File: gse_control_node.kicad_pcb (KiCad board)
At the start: 4 copper layers, 65 x 65 mm, 119 parts, among them J1 Screw_Terminal_01x02, J10 Conn_01x02, J2 Conn_01x04, J3 Conn_01x04, J4 Conn_02x01, J5 USB_C_Receptacle_USB2.0_16P, J6 Conn_01x04, J7 Conn_01x02, J8 Conn_01x02, J9 Conn_01x02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

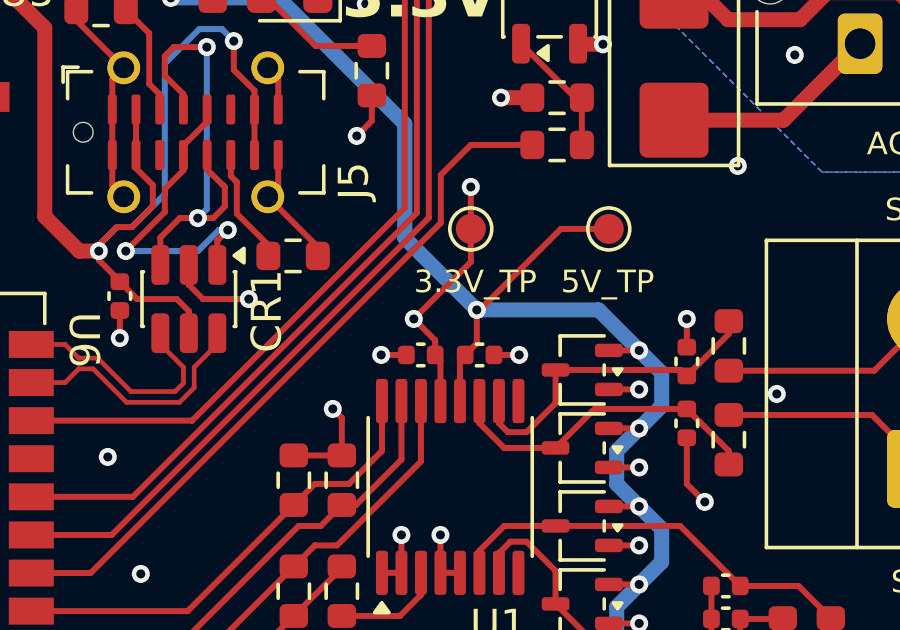
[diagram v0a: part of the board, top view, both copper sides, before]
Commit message: move up ads112c04 capacitors further from pins for easier handsoldering
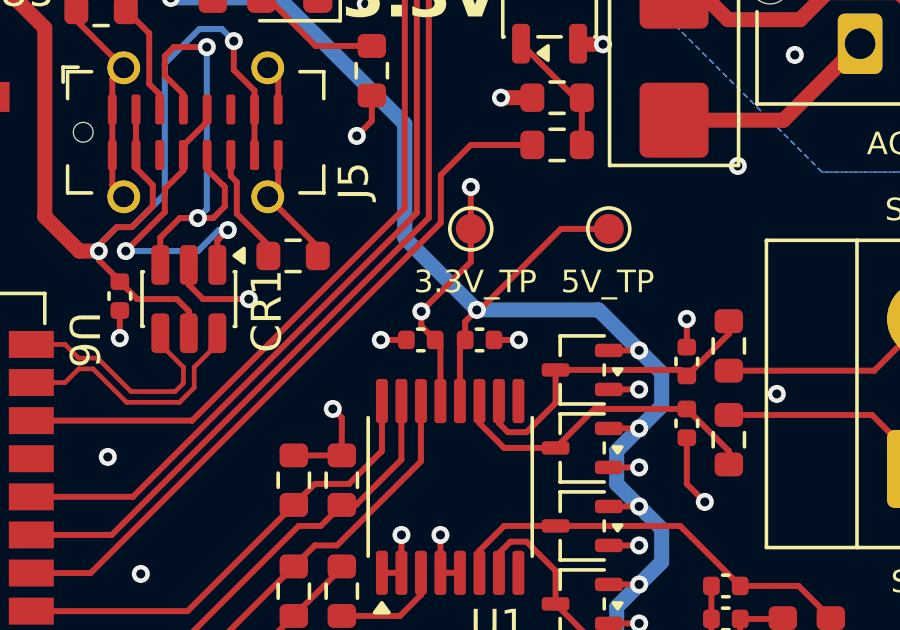
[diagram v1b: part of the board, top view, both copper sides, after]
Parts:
- moved C1 0.50 mm to (106.0, 63.5)
- moved C2 0.50 mm to (108.0, 63.5)
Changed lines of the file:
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@@
 	(footprint "Capacitor_SMD:C_0402_1005Metric"
 		(layer "F.Cu")
-		(at 107.992499 64)
+		(at 107.992499 63.5)
 		(descr "Capacitor SMD 0402 (1005 Metric), square (rectangular) end terminal, IPC-7351 nominal, (Body size source: IPC-SM-782 page 76, https://www.pcb-3d.com/wordpress/wp-content/uploads/ipc-sm-782a_amendment_1_and_2.pdf)")
 		(tags "capacitor")
@@
 	(footprint "Capacitor_SMD:C_0402_1005Metric"
 		(layer "F.Cu")
-		(at 106.032499 64 180)
+		(at 106.032499 63.5 180)
 		(descr "Capacitor SMD 0402 (1005 Metric), square (rectangular) end terminal, IPC-7351 nominal, (Body size source: IPC-SM-782 page 76, https://www.pcb-3d.com/wordpress/wp-content/uploads/ipc-sm-782a_amendment_1_and_2.pdf)")
 		(tags "capacitor")
@@
 	)
 	(segment
+		(start 108.472499 63.5)
+		(end 109.3 63.5)
+		(width 0.2)
+		(layer "F.Cu")
+		(net "GND")
+	)
+	(segment
 		(start 112.299999 67.75)
 		(end 113.312499 67.75)
@@
 	)
 	(segment
-		(start 105.552499 64)
-		(end 104.712499 64)
-		(width 0.2)
-		(layer "F.Cu")
-		(net "GND")
-	)
-	(segment
 		(start 114.9 63.74)
 		(end 114.9 62.8)
@@
 	)
 	(segment
-		(start 108.472499 64)
-		(end 109.312499 64)
-		(width 0.2)
-		(layer "F.Cu")
-		(net "GND")
-	)
-	(segment
 		(start 100.93 54.427918)
 		(end 101.28 54.777918)
@@
 	)
 	(segment
+		(start 105.552499 63.5)
+		(end 104.7 63.5)
+		(width 0.2)
+		(layer "F.Cu")
+		(net "GND")
+	)
+	(segment
 		(start 84.52 51.8)
 		(end 86 51.8)
@@
 	)
 	(via
+		(at 104.7 63.5)
+		(size 0.6)
+		(drill 0.3)
+		(layers "F.Cu" "B.Cu")
+		(net "GND")
+	)
+	(via
 		(at 73.7 66.1)
 		(size 0.6)
@@
 	)
 	(via
-		(at 104.712499 64)
-		(size 0.6)
-		(drill 0.3)
-		(layers "F.Cu" "B.Cu")
-		(net "GND")
-	)
-	(via
 		(at 99.1 79.57)
 		(size 0.6)
@@
 	)
 	(via
+		(at 109.3 63.5)
+		(size 0.6)
+		(drill 0.3)
+		(layers "F.Cu" "B.Cu")
+		(net "GND")
+	)
+	(via
 		(at 116.6 40.7)
 		(size 0.6)
@@
 	)
 	(via
-		(at 109.312499 64)
-		(size 0.6)
-		(drill 0.3)
-		(layers "F.Cu" "B.Cu")
-		(net "GND")
-	)
-	(via
 		(at 109.4 22)
 		(size 0.6)
@@
 	)
 	(segment
-		(start 107.9 62.5)
-		(end 107.9 63.612499)
+		(start 107.337499 65.5375)
+		(end 107.337499 63.675)
 		(width 0.2)
 		(layer "F.Cu")
@@
 	)
 	(segment
-		(start 112.299999 66.45)
-		(end 113.312499 66.45)
+		(start 107.337499 63.675)
+		(end 107.512499 63.5)
 		(width 0.2)
 		(layer "F.Cu")
@@
 	)
 	(segment
-		(start 107.337499 65.5375)
-		(end 107.337499 64.175)
+		(start 112.299999 66.45)
+		(end 113.312499 66.45)
 		(width 0.2)
 		(layer "F.Cu")
@@
 	)
 	(segment
+		(start 107.512499 62.887501)
+		(end 107.9 62.5)
+		(width 0.2)
+		(layer "F.Cu")
+		(net "+5V")
+	)
+	(segment
 		(start 98.475 51.325)
 		(end 97.7 52.1)
@@
 	)
 	(segment
-		(start 107.337499 64.175)
-		(end 107.512499 64)
+		(start 107.512499 63.5)
+		(end 107.512499 62.887501)
 		(width 0.2)
 		(layer "F.Cu")
@@
 	)
 	(segment
-		(start 107.9 63.612499)
-		(end 107.512499 64)
-		(width 0.2)
-		(layer "F.Cu")
-		(net "+5V")
-	)
-	(segment
 		(start 97.3 48.55)
 		(end 98.475 49.725)
@@
 	)
 	(segment
-		(start 71.704958 49.925)
-		(end 71.704958 50.704958)
+		(start 106.687499 63.675)
+		(end 106.512499 63.5)
 		(width 0.2)
 		(layer "F.Cu")
@@
 	)
 	(segment
-		(start 106.687499 64.175)
-		(end 106.512499 64)
+		(start 106.05 62.55)
+		(end 107.7 60.9)
+		(width 0.2)
+		(layer "F.Cu")
+		(net "+3.3V")
+	)
+	(segment
+		(start 71.704958 49.925)
+		(end 71.704958 50.704958)
 		(width 0.2)
 		(layer "F.Cu")
@@
 	)
 	(segment
-		(start 73.7 52.7)
-		(end 79.8 52.7)
+		(start 106.687499 65.5375)
+		(end 106.687499 63.675)
 		(width 0.2)
 		(layer "F.Cu")
@@
 	)
 	(segment
-		(start 106.687499 65.5375)
-		(end 106.687499 64.175)
+		(start 73.7 52.7)
+		(end 79.8 52.7)
 		(width 0.2)
 		(layer "F.Cu")
@@
 	)
 	(segment
-		(start 106.512499 63.512499)
-		(end 105.8 62.8)
+		(start 106.05 63.037501)
+		(end 106.512499 63.5)
 		(width 0.2)
 		(layer "F.Cu")
@@
 	)
 	(segment
-		(start 107.7 59.8)
-		(end 107.7 60.9)
+		(start 94.635 78.91)
+		(end 94.715 78.99)
 		(width 0.2)
 		(layer "F.Cu")
@@
 	)
 	(segment
-		(start 94.635 78.91)
-		(end 94.715 78.99)
+		(start 107.7 60.9)
+		(end 107.7 59.8)
 		(width 0.2)
 		(layer "F.Cu")
@@
 	)
 	(segment
-		(start 107.7 60.9)
-		(end 105.8 62.8)
+		(start 106.05 62.55)
+		(end 106.05 63.037501)
 		(width 0.2)
 		(layer "F.Cu")
@@
 	)
 	(segment
-		(start 106.512499 64)
-		(end 106.512499 63.512499)
-		(width 0.2)
-		(layer "F.Cu")
-		(net "+3.3V")
-	)
-	(segment
 		(start 104.4 55.35)
 		(end 104.4 56.2)
@@
 	)
 	(via
-		(at 105.8 62.8)
+		(at 106.05 62.55)
 		(size 0.6)
 		(drill 0.3)
@@
 		(members "0713b475-f5cb-4c27-85e3-ad1de07ab9aa" "077e1e74-6f91-4637-9c72-50ae116940d0"
 			"09fb94bb-8471-4aec-ad5d-a9e6f7ed850c" "143357c3-ebe5-4e68-bb4f-053ab14f5365"
-			"1611942c-b6f4-400d-942c-48b3fd8efb8b" "2002362c-b7c0-435e-b928-a278ebd1ba91"
-			"254d465c-a598-4fa1-838f-c53555367d58" "26810a1b-9afc-4230-aa9a-717d25e7bf46"
+			"1611942c-b6f4-400d-942c-48b3fd8efb8b" "18de1a66-394e-45ff-8f65-4990c2640ed2"
+			"2002362c-b7c0-435e-b928-a278ebd1ba91" "26810a1b-9afc-4230-aa9a-717d25e7bf46"
 			"272b0b43-69c4-45c3-a902-39b13e856481" "3392c1c7-c6f3-47a8-a50d-0791db8bd6ba"
 			"35487309-e541-48d0-83e2-fdf5931405a9" "398871a5-91ec-4523-b6c2-31a6d168fd13"
 			"3992ca7f-4747-4014-b0d3-b52654d03022" "3a4d2a50-53e1-4501-b2b1-020b92b24701"
-			"4031506d-cd5c-474b-aded-242a9de5b808" "4bb322c4-beaa-4428-8206-724f55f07d49"
+			"3ca64c91-c041-451d-aa41-0b8179a51e5b" "4031506d-cd5c-474b-aded-242a9de5b808"
+			"4ae5ce71-c6d8-4e7c-b337-34813efee1bc" "4bb322c4-beaa-4428-8206-724f55f07d49"
 			"520842bf-d7f1-45f1-a857-1e2e2b3e0304" "53271790-ca79-482e-aa70-61861ad501a4"
 			"5ac32f9c-315f-4e1c-86a3-f0cc58c834f3" "5ba14bdf-6ad9-4dd0-868b-07183184e65b"
 			"60ee43a8-b7f1-4438-ace5-67193ee89a17" "6a3f31a3-fe63-4587-9a30-071251119eca"
 			"6b6c3120-d685-45bb-883f-7689f5c635ba" "77c11dec-9216-45a1-beb1-ecd6b7c83a28"
-			"79d439f1-bc39-4da3-8bfa-e40741087e2c" "7f6941e2-e005-46d9-a4d8-e668f29aadfa"
-			"7fb87c2d-13ab-42b9-a622-50f20d7c8d91" "85811859-a147-483f-ae9c-36d4455d3eb6"
+			"79d439f1-bc39-4da3-8bfa-e40741087e2c" "7fb87c2d-13ab-42b9-a622-50f20d7c8d91"
+			"813fed4b-3560-48dc-b9dc-4773828fcd3b" "85811859-a147-483f-ae9c-36d4455d3eb6"
 			"874789a6-e4f6-4d20-96b9-63f47ce8a054" "89242e3a-437f-4c51-836e-c2bfc0d14e6b"
-			"8c5af611-fac6-4ee7-9db9-3087e55b4cbc" "9520423f-e2b5-4333-b303-308e31356465"
-			"9679f33c-0414-4287-bc77-a4bfba0f9619" "972f63cd-ad98-4fb9-bbfb-7680c819cf8f"
-			"97ef5fcd-715e-4292-849d-59b79a742a7d" "99416f0b-bd1e-450c-9a2d-39476234f809"
-			"99a3ca92-a9b4-4f3a-8894-e1c4da141f22" "9a605955-d230-4d70-9ac7-4ab602a980e3"
-			"a047faab-255e-4ef1-bdc6-788e9bc43326" "a1ecc4fa-a627-4f55-9ba0-37c7803925a8"
+			"8b92bc17-2e35-45b4-ac6d-edc5b158a71e" "9520423f-e2b5-4333-b303-308e31356465"
+			"9679f33c-0414-4287-bc77-a4bfba0f9619" "97ef5fcd-715e-4292-849d-59b79a742a7d"
+			"99416f0b-bd1e-450c-9a2d-39476234f809" "99a3ca92-a9b4-4f3a-8894-e1c4da141f22"
+			"9a605955-d230-4d70-9ac7-4ab602a980e3" "a047faab-255e-4ef1-bdc6-788e9bc43326"
 			"a93fd3e5-3a84-4405-ae40-05b572e65529" "a9b2d57a-f670-4513-b9c0-c2dc32cccd4e"
-			"aa20b915-049c-41ac-bf38-724fe6be948c" "aff2acdf-d84c-4d91-859b-550af43d1e9b"
+			"ad331356-d70b-4977-b70c-951d6688ec29" "aff2acdf-d84c-4d91-859b-550af43d1e9b"
 			"b0897651-7570-48f1-acde-4cc7863531c8" "bac0bc6e-03ea-4ccd-a2d3-603e4a49b3d7"
-			"bdf58728-7c54-4d66-8e71-7c2b8beb86f8" "c3e717e2-7834-47ee-ac64-8a312146c262"
-			"c494923c-e162-4fc7-a0e4-078a73375c22" "c52fd37b-f8b4-4782-bbd6-512d36cd1355"
-			"c5ae6679-79b9-4580-9dbc-c82893933102" "c667d184-ed5d-4410-9b14-25c8bdc7dc27"
-			"c784093f-aa9b-4f53-902b-9be59066781f" "c85fb981-ea2f-4e3b-af4e-8b51bd8042af"
-			"c93e094e-23ad-4496-a67c-0f8ea6effcd8" "cc0d71a9-384e-4854-bdc0-0d0361614c1a"
-			"cdb0dd8d-516c-49c6-8032-b546fb987add" "d0cbf0f5-bd98-42b9-baca-ec8107ff06dc"
-			"d2acdac1-c997-4b5b-92bd-a9f6b2d041a3" "d6f2acbf-eac1-48da-b50e-1cdd310e12a0"
-			"d89bfdb0-187b-4b25-a7b7-b023acbaa4b4" "da27c5d9-14f2-48bc-81b8-29e3cf13fe25"
-			"dcbbba95-6765-4085-874d-df7959760735" "e5ad27bf-e527-44fb-aa32-76ae20692841"
+			"bdf58728-7c54-4d66-8e71-7c2b8beb86f8" "c00c2267-045f-4dc7-8730-456783d7cecc"
+			"c3e717e2-7834-47ee-ac64-8a312146c262" "c494923c-e162-4fc7-a0e4-078a73375c22"
+			"c52fd37b-f8b4-4782-bbd6-512d36cd1355" "c5ae6679-79b9-4580-9dbc-c82893933102"
+			"c667d184-ed5d-4410-9b14-25c8bdc7dc27" "c784093f-aa9b-4f53-902b-9be59066781f"
+			"c85fb981-ea2f-4e3b-af4e-8b51bd8042af" "c93e094e-23ad-4496-a67c-0f8ea6effcd8"
+			"cc0d71a9-384e-4854-bdc0-0d0361614c1a" "cdb0dd8d-516c-49c6-8032-b546fb987add"
+			"d0cbf0f5-bd98-42b9-baca-ec8107ff06dc" "d2acdac1-c997-4b5b-92bd-a9f6b2d041a3"
+			"d6f2acbf-eac1-48da-b50e-1cdd310e12a0" "d89bfdb0-187b-4b25-a7b7-b023acbaa4b4"
+			"da27c5d9-14f2-48bc-81b8-29e3cf13fe25" "dcbbba95-6765-4085-874d-df7959760735"
 			"e70306a6-08d0-488c-bf4f-7f69efa03470" "e85a9e07-8c9b-44bd-915f-96d6cd51afa4"
-			"e91782cf-deaf-4542-8095-f2d6c775d17d" "eea5b277-e46b-4c3b-8d5c-9d3e61cdf2b4"
-			"ef3803de-90ad-46b6-948b-407f3d22f1e5" "eff16b14-496b-40bc-aeac-67ec399e5917"
+			"e91782cf-deaf-4542-8095-f2d6c775d17d" "eba4b831-4452-40f2-92b8-bd84efb44e80"
+			"eea5b277-e46b-4c3b-8d5c-9d3e61cdf2b4" "ef3803de-90ad-46b6-948b-407f3d22f1e5"
 			"f3b3eb13-9123-49bc-9c49-2970c895796b" "f907aad5-5490-49da-a093-8d0a827d9643"
 			"ff226c3a-8f29-4d59-b294-a520e485934e" "ffae27af-3de5-47aa-a534-f03b9ce38791"

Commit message: remove some extended components from bom (to be handsoldered)
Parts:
- moved G*** 49.2 mm to (88.0, 73.9)
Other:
- board text added: "GSE Control Node"
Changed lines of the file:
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@@
 			)
 		)
-		(attr smd)
+		(attr smd exclude_from_pos_files exclude_from_bom)
 		(duplicate_pad_numbers_are_jumpers no)
 		(fp_line
@@
 			)
 		)
-		(attr smd)
+		(attr smd exclude_from_pos_files exclude_from_bom)
 		(duplicate_pad_numbers_are_jumpers no)
 		(fp_line
@@
 			)
 		)
-		(attr smd)
+		(attr smd exclude_from_pos_files exclude_from_bom)
 		(duplicate_pad_numbers_are_jumpers no)
 		(fp_line
@@
 			)
 		)
-		(attr smd)
+		(attr smd exclude_from_pos_files exclude_from_bom)
 		(duplicate_pad_numbers_are_jumpers no)
 		(fp_line
@@
 			)
 		)
-		(attr smd)
+		(attr smd exclude_from_pos_files exclude_from_bom)
 		(duplicate_pad_numbers_are_jumpers no)
 		(fp_line
@@
 			)
 		)
-		(attr smd)
+		(attr smd exclude_from_pos_files exclude_from_bom)
 		(duplicate_pad_numbers_are_jumpers no)
 		(fp_line
@@
 			)
 		)
-		(attr smd)
+		(attr smd exclude_from_pos_files exclude_from_bom)
 		(duplicate_pad_numbers_are_jumpers no)
 		(fp_line
@@
 			)
 		)
-		(attr smd)
+		(attr smd exclude_from_pos_files exclude_from_bom)
 		(duplicate_pad_numbers_are_jumpers no)
 		(fp_line
@@
 			)
 		)
-		(attr smd)
+		(attr smd exclude_from_pos_files exclude_from_bom)
 		(duplicate_pad_numbers_are_jumpers no)
 		(fp_line
@@
 			)
 		)
-		(attr smd)
+		(attr smd exclude_from_pos_files exclude_from_bom)
 		(duplicate_pad_numbers_are_jumpers no)
 		(fp_line
@@
 			)
 		)
-		(attr smd)
+		(attr smd exclude_from_pos_files exclude_from_bom)
 		(duplicate_pad_numbers_are_jumpers no)
 		(fp_line
@@
 			)
 		)
-		(attr smd)
+		(attr smd exclude_from_pos_files exclude_from_bom)
 		(duplicate_pad_numbers_are_jumpers no)
 		(fp_line
@@
 			)
 		)
-		(attr smd)
+		(attr smd exclude_from_pos_files exclude_from_bom)
 		(duplicate_pad_numbers_are_jumpers no)
 		(fp_line
@@
 			)
 		)
-		(attr smd)
+		(attr smd exclude_from_pos_files exclude_from_bom)
 		(duplicate_pad_numbers_are_jumpers no)
 		(fp_line
@@
 			)
 		)
-		(attr smd)
+		(attr smd exclude_from_pos_files exclude_from_bom)
 		(duplicate_pad_numbers_are_jumpers no)
 		(fp_line
@@
 			)
 		)
-		(attr smd)
+		(attr smd exclude_from_pos_files exclude_from_bom)
 		(duplicate_pad_numbers_are_jumpers no)
 		(fp_line
@@
 			)
 		)
-		(attr smd)
+		(attr smd exclude_from_pos_files exclude_from_bom)
 		(duplicate_pad_numbers_are_jumpers no)
 		(fp_line
@@
 			)
 		)
-		(attr smd)
+		(attr smd exclude_from_pos_files exclude_from_bom)
 		(duplicate_pad_numbers_are_jumpers no)
 		(fp_line
@@
 			)
 		)
-		(attr smd)
+		(attr smd exclude_from_pos_files exclude_from_bom)
 		(duplicate_pad_numbers_are_jumpers no)
 		(fp_line
@@
 			)
 		)
-		(attr smd)
+		(attr smd exclude_from_pos_files exclude_from_bom)
 		(duplicate_pad_numbers_are_jumpers no)
 		(fp_line
@@
 	(footprint "LOGO"
 		(layer "B.Cu")
-		(at 96.9 25.5 180)
+		(at 88.029475 73.912293 180)
 		(property "Reference" "G***"
 			(at 0 0 0)
@@
 			)
 			(justify left bottom mirror)
+		)
+	)
+	(gr_text "GSE Control Node"
+		(at 106.7 21.2 0)
+		(layer "B.SilkS")
+		(effects
+			(font
+				(size 1.5 1.5)
+				(thickness 0.3)
+				(bold yes)
+			)
+			(justify left bottom mirror)

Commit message: update screw terminal footprint
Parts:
- J1: footprint TerminalBlock_Phoenix:TerminalBlock_Phoenix_MKDS-1,5-2_1x02_P5.00mm_Horizontal -> TerminalBlock_CUI:TerminalBlock_CUI_TB007-508-02_1x02_P5.08mm_Horizontal
- moved C4 0.38 mm to (114.5, 66.3)
- moved C6 0.38 mm to (114.5, 64.2)
- moved J1 0.38 mm to (122.5, 67.8)
- moved R6 0.38 mm to (115.9, 63.7)
- moved R7 0.38 mm to (115.9, 66.8)
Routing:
- net GND: track 78.0 -> 77.3 mm, vias 107 -> 106

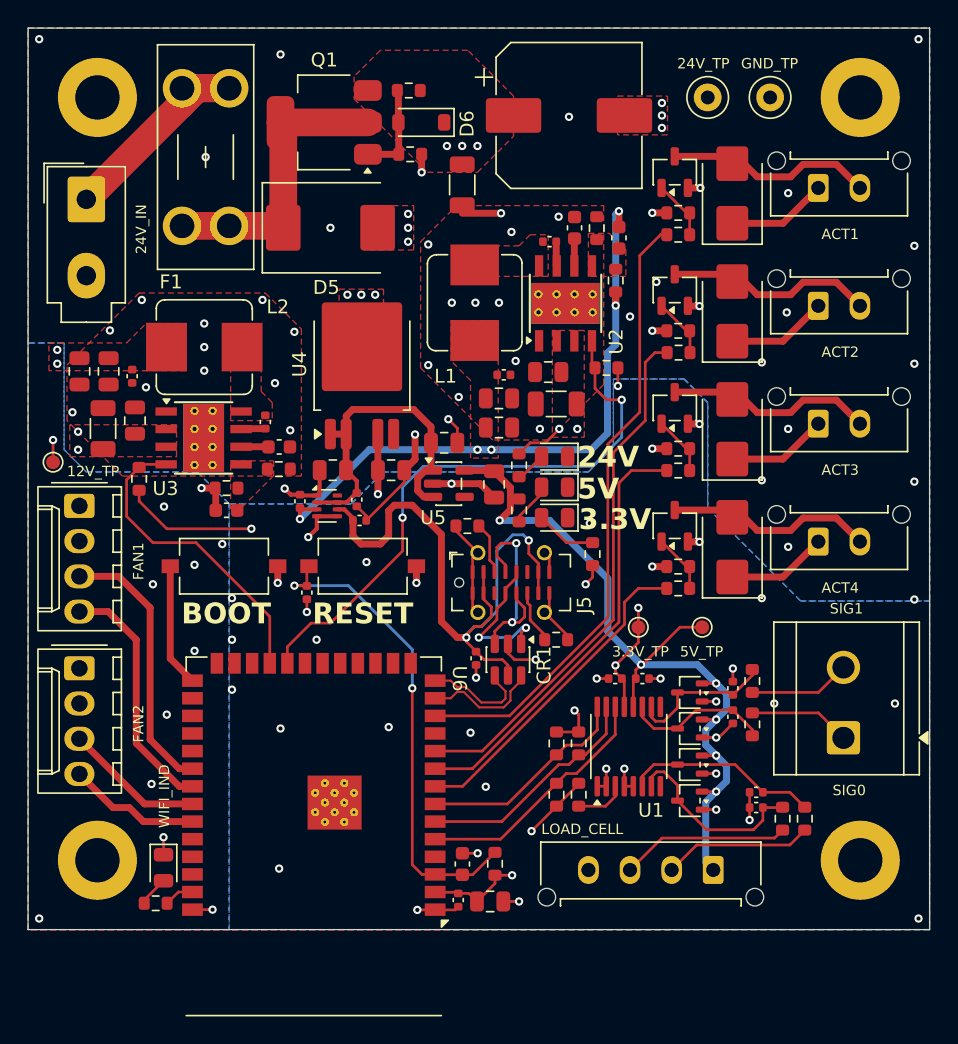
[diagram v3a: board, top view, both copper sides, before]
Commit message: add tachometer pullup and pwm low side fet for fans
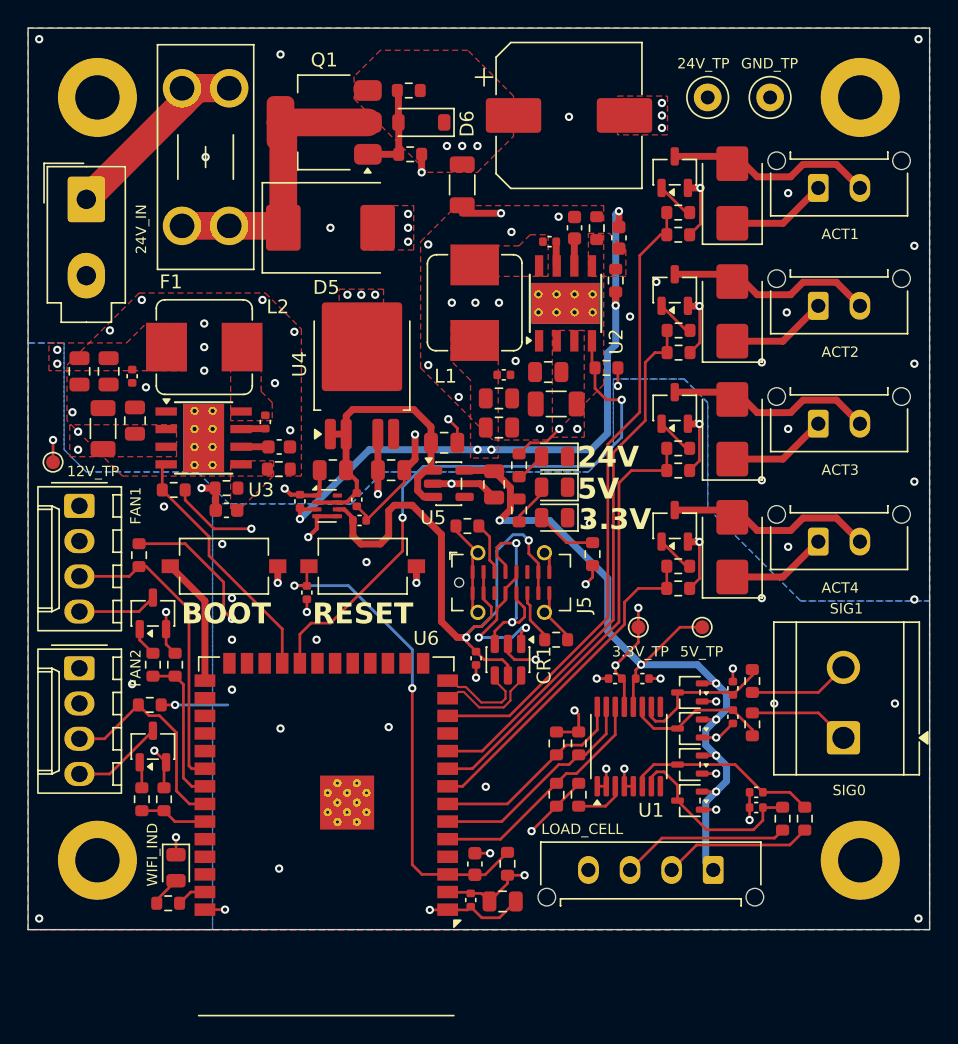
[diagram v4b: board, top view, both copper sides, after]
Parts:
- added Q6: BSS138, Package_TO_SOT_SMD:SOT-23-3, F.Cu at (72.7, 58.8)
- added Q7: BSS138, Package_TO_SOT_SMD:SOT-23-3, F.Cu at (72.7, 68.4)
- added R32: 10kΩ, Resistor_SMD:R_0603_1608Metric, F.Cu at (71.7, 54.6)
- added R33: 10kΩ, Resistor_SMD:R_0603_1608Metric, F.Cu at (72.5, 65.4)
- added R34: 100Ω, Resistor_SMD:R_0603_1608Metric, F.Cu at (72.7, 62.5)
- added R35: 100kΩ, Resistor_SMD:R_0603_1608Metric, F.Cu at (74.3, 62.5)
- added R36: 100Ω, Resistor_SMD:R_0603_1608Metric, F.Cu at (71.9, 72.2)
- added R37: 100kΩ, Resistor_SMD:R_0603_1608Metric, F.Cu at (73.5, 72.2)
- moved R11 2.62 mm to (74.2, 49.9), turned to 0 degrees
- moved R24 1.60 mm to (110.6, 29.9)
- moved R26 1.60 mm to (110.6, 38.4)
- moved R28 1.60 mm to (110.6, 46.9)
- moved R30 1.60 mm to (110.6, 55.4)
- moved R27 1.58 mm to (110.6, 40.0), turned to 0 degrees
- moved R29 1.58 mm to (110.6, 48.5), turned to 0 degrees
- moved R31 1.58 mm to (110.6, 57.0), turned to 0 degrees
- moved R25 1.57 mm to (110.6, 31.5), turned to 0 degrees
- moved C29 0.90 mm to (97.9, 79.6)
- moved C31 0.90 mm to (95.9, 76.9)
- moved R20 0.90 mm to (98.3, 76.9)
- moved U6 0.90 mm to (85.2, 74.9)
- moved C30 0.90 mm to (95.6, 79.5)
- moved D10 0.90 mm to (74.4, 77.1)
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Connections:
- J2 pad 4: FAN_1_PWM -> Net-(J2-Pin_4)
- J6 pad 4: FAN_2_PWM -> Net-(J6-Pin_4)
- R25 pad 1: Net-(Q2-G) -> ACTUATOR_1_CTL
- R27 pad 1: Net-(Q3-G) -> ACTUATOR_2_CTL
- R29 pad 1: Net-(Q4-G) -> ACTUATOR_3_CTL
- R31 pad 1: Net-(Q5-G) -> ACTUATOR_4_CTL
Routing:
- net GND: track 77.3 -> 97.0 mm, vias 106 -> 98
- net +3.3V: track 40.0 -> 51.7 mm, vias 9 -> 11
- net FAN_1_PWM: track 17.7 -> 11.0 mm
- net Net-(J6-Pin_4): track 0.00 -> 6.59 mm
- net Net-(J2-Pin_4): track 0.00 -> 5.72 mm
- net FAN_2_TACH: track 10.1 -> 15.5 mm
- net FAN_2_PWM: track 9.57 -> 4.88 mm
- net 12V_PG: track 22.6 -> 18.0 mm
- net FAN_1_TACH: track 19.5 -> 22.0 mm
- net Net-(Q6-G): track 0.00 -> 2.13 mm
- net Net-(Q7-G): track 0.00 -> 1.90 mm
- net Net-(Q5-G): track 4.35 -> 2.76 mm
- net Net-(Q2-G): track 4.35 -> 2.76 mm
- net Net-(Q3-G): track 4.36 -> 2.79 mm
- net Net-(Q4-G): track 4.35 -> 2.99 mm
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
